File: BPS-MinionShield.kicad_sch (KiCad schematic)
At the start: 78 parts, among them J1 TempConn1, J2 TempConn2, J3 Conn_01x24_Female

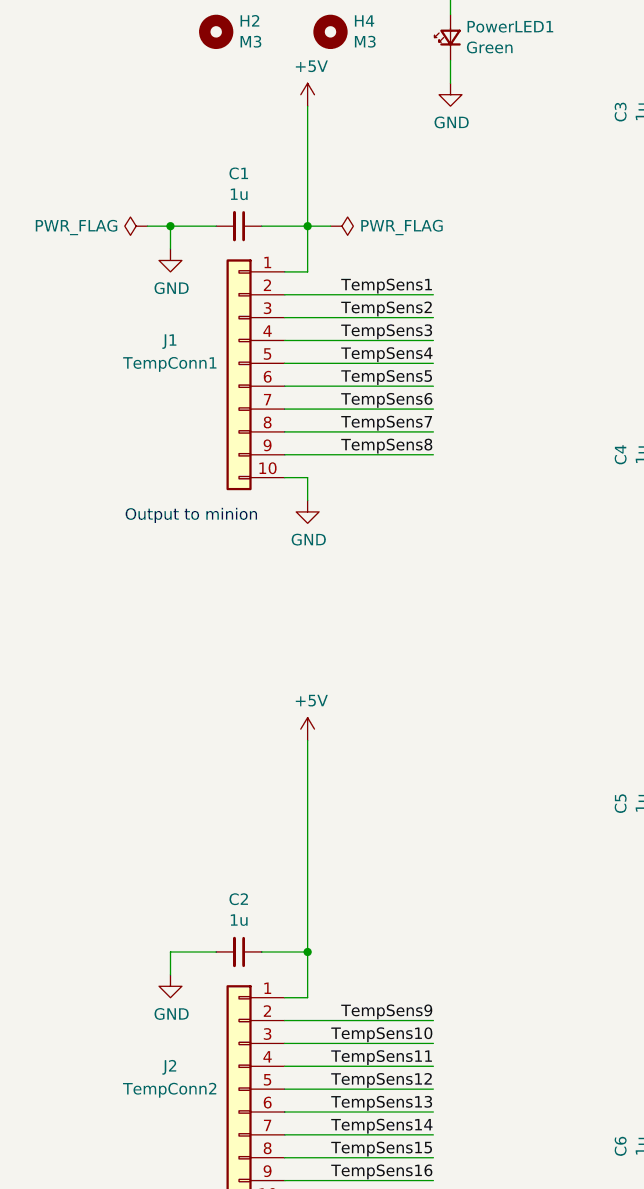
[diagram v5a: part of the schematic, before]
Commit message: move ferrite beads away from connector
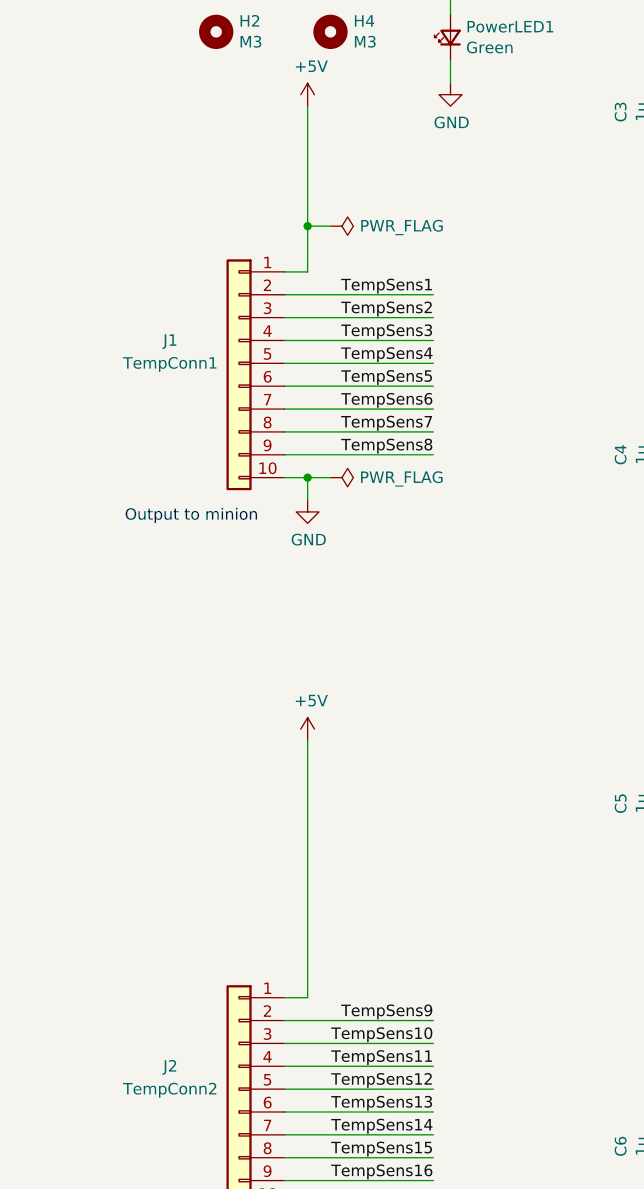
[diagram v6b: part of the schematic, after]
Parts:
- removed C1, C2: 1u, Capacitor_SMD:C_0805_2012Metric_Pad1.18x1.45mm_HandSolder, symbol Device:C_Small
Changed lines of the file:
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@@
   (junction (at 184.15 35.56) (diameter 0) (color 0 0 0 0)
   )
-  (junction (at 48.26 133.985) (diameter 0) (color 0 0 0 0)
-  )
   (junction (at 88.9 73.66) (diameter 0) (color 0 0 0 0)
   )
@@
   (junction (at 152.4 35.56) (diameter 0) (color 0 0 0 0)
   )
-  (junction (at 33.02 53.34) (diameter 0) (color 0 0 0 0)
-  )
   (junction (at 152.4 150.495) (diameter 0) (color 0 0 0 0)
   )
@@
   )
   (junction (at 164.465 35.56) (diameter 0) (color 0 0 0 0)
+  )
+  (junction (at 48.26 81.28) (diameter 0) (color 0 0 0 0)
   )
   (junction (at 229.235 127) (diameter 0) (color 0 0 0 0)
@@
     (stroke (width 0) (type default) (color 0 0 0 0))
   )
-  (wire (pts (xy 33.02 133.985) (xy 33.02 136.525))
-    (stroke (width 0) (type default) (color 0 0 0 0))
-  )
-  (wire (pts (xy 33.02 53.34) (xy 33.02 55.88))
-    (stroke (width 0) (type default) (color 0 0 0 0))
-  )
   (wire (pts (xy 132.715 150.495) (xy 135.255 150.495))
     (stroke (width 0) (type default) (color 0 0 0 0))
@@
     (stroke (width 0) (type default) (color 0 0 0 0))
   )
-  (wire (pts (xy 30.48 53.34) (xy 33.02 53.34))
+  (wire (pts (xy 50.8 81.28) (xy 48.26 81.28))
     (stroke (width 0) (type default) (color 0 0 0 0))
   )
@@
     (stroke (width 0) (type default) (color 0 0 0 0))
   )
-  (wire (pts (xy 48.26 133.985) (xy 48.26 139.065))
-    (stroke (width 0) (type default) (color 0 0 0 0))
-  )
   (wire (pts (xy 91.44 112.395) (xy 88.9 112.395))
     (stroke (width 0) (type default) (color 0 0 0 0))
@@
     (stroke (width 0) (type default) (color 0 0 0 0))
   )
-  (wire (pts (xy 48.26 53.34) (xy 43.18 53.34))
-    (stroke (width 0) (type default) (color 0 0 0 0))
-  )
   (wire (pts (xy 152.4 73.66) (xy 152.4 76.2))
     (stroke (width 0) (type default) (color 0 0 0 0))
@@
     (stroke (width 0) (type default) (color 0 0 0 0))
   )
-  (wire (pts (xy 48.26 133.985) (xy 43.18 133.985))
-    (stroke (width 0) (type default) (color 0 0 0 0))
-  )
   (wire (pts (xy 99.06 73.66) (xy 100.965 73.66))
     (stroke (width 0) (type default) (color 0 0 0 0))
@@
     (stroke (width 0) (type default) (color 0 0 0 0))
   )
-  (wire (pts (xy 48.26 110.49) (xy 48.26 133.985))
+  (wire (pts (xy 48.26 110.49) (xy 48.26 139.065))
     (stroke (width 0) (type default) (color 0 0 0 0))
   )
@@
     (stroke (width 0) (type default) (color 0 0 0 0))
   )
-  (wire (pts (xy 38.1 133.985) (xy 33.02 133.985))
-    (stroke (width 0) (type default) (color 0 0 0 0))
-  )
   (wire (pts (xy 164.465 35.56) (xy 167.005 35.56))
     (stroke (width 0) (type default) (color 0 0 0 0))
@@
   )
   (wire (pts (xy 88.9 35.56) (xy 88.9 38.1))
-    (stroke (width 0) (type default) (color 0 0 0 0))
-  )
-  (wire (pts (xy 38.1 53.34) (xy 33.02 53.34))
     (stroke (width 0) (type default) (color 0 0 0 0))
   )
@@
     (pin "1")
   )
-  (symbol (lib_id "power:GND") (at 33.02 136.525 0) (unit 1)
-    (in_bom yes) (on_board yes)
-    (property "Reference" "#PWR02" (id 0) (at 33.02 142.875 0)
-      (effects (font (size 1.27 1.27)) hide)
-    )
-    (property "Value" "GND" (id 1) (at 33.147 140.9192 0))
-    (property "Footprint" "" (id 2) (at 33.02 136.525 0)
-      (effects (font (size 1.27 1.27)) hide)
-    )
-    (property "Datasheet" "" (id 3) (at 33.02 136.525 0)
-      (effects (font (size 1.27 1.27)) hide)
-    )
-    (pin "1")
-  )
   (symbol (lib_id "Connector_Generic:Conn_01x10") (at 40.64 68.58 0) (mirror y) (unit 1)
     (in_bom yes) (on_board yes)
@@
     (pin "9")
   )
-  (symbol (lib_id "Device:C_Small") (at 40.64 53.34 270) (unit 1)
-    (in_bom yes) (on_board yes)
-    (property "Reference" "C1" (id 0) (at 40.64 47.5234 90))
-    (property "Value" "1u" (id 1) (at 40.64 49.8348 90))
-    (property "Footprint" "Capacitor_SMD:C_0805_2012Metric_Pad1.18x1.45mm_HandSolder" (id 2) (at 40.64 53.34 0)
-      (effects (font (size 1.27 1.27)) hide)
-    )
-    (property "Datasheet" "https://www.mouser.com/ProductDetail/KEMET/C0805C104K5RAC?qs=r%2FVmNO8Tjq4%2F8ymSnGP6Jw%3D%3D" (id 3) (at 40.64 53.34 0)
-      (effects (font (size 1.27 1.27)) hide)
-    )
-    (pin "1")
-    (pin "2")
-  )
-  (symbol (lib_id "power:GND") (at 33.02 55.88 0) (unit 1)
-    (in_bom yes) (on_board yes)
-    (property "Reference" "#PWR01" (id 0) (at 33.02 62.23 0)
-      (effects (font (size 1.27 1.27)) hide)
-    )
-    (property "Value" "GND" (id 1) (at 33.147 60.2742 0))
-    (property "Footprint" "" (id 2) (at 33.02 55.88 0)
-      (effects (font (size 1.27 1.27)) hide)
-    )
-    (property "Datasheet" "" (id 3) (at 33.02 55.88 0)
-      (effects (font (size 1.27 1.27)) hide)
-    )
-    (pin "1")
-  )
   (symbol (lib_id "power:GND") (at 48.26 83.82 0) (unit 1)
     (in_bom yes) (on_board yes)
@@
     (pin "1")
   )
-  (symbol (lib_id "power:PWR_FLAG") (at 30.48 53.34 90) (unit 1)
-    (in_bom yes) (on_board yes)
-    (property "Reference" "#FLG01" (id 0) (at 28.575 53.34 0)
-      (effects (font (size 1.27 1.27)) hide)
-    )
-    (property "Value" "PWR_FLAG" (id 1) (at 27.2542 53.34 90)
+  (symbol (lib_id "power:PWR_FLAG") (at 50.8 81.28 270) (unit 1)
+    (in_bom yes) (on_board yes)
+    (property "Reference" "#FLG01" (id 0) (at 52.705 81.28 0)
+      (effects (font (size 1.27 1.27)) hide)
+    )
+    (property "Value" "PWR_FLAG" (id 1) (at 54.0258 81.28 90)
       (effects (font (size 1.27 1.27)) (justify left))
     )
-    (property "Footprint" "" (id 2) (at 30.48 53.34 0)
-      (effects (font (size 1.27 1.27)) hide)
-    )
-    (property "Datasheet" "~" (id 3) (at 30.48 53.34 0)
+    (property "Footprint" "" (id 2) (at 50.8 81.28 0)
+      (effects (font (size 1.27 1.27)) hide)
+    )
+    (property "Datasheet" "~" (id 3) (at 50.8 81.28 0)
       (effects (font (size 1.27 1.27)) hide)
     )
@@
     (pin "2")
   )
-  (symbol (lib_id "Device:C_Small") (at 40.64 133.985 270) (unit 1)
-    (in_bom yes) (on_board yes)
-    (property "Reference" "C2" (id 0) (at 40.64 128.1684 90))
-    (property "Value" "1u" (id 1) (at 40.64 130.4798 90))
-    (property "Footprint" "Capacitor_SMD:C_0805_2012Metric_Pad1.18x1.45mm_HandSolder" (id 2) (at 40.64 133.985 0)
-      (effects (font (size 1.27 1.27)) hide)
-    )
-    (property "Datasheet" "https://www.mouser.com/ProductDetail/KEMET/C0805C104K5RAC?qs=r%2FVmNO8Tjq4%2F8ymSnGP6Jw%3D%3D" (id 3) (at 40.64 133.985 0)
-      (effects (font (size 1.27 1.27)) hide)
-    )
-    (pin "1")
-    (pin "2")
-  )
   (symbol (lib_id "power:GND") (at 152.4 45.72 0) (unit 1)
     (in_bom yes) (on_board yes)
@@
       (reference "#FLG02") (unit 1) (value "PWR_FLAG") (footprint "")
     )
-    (path "/00000000-0000-0000-0000-00005db6d147"
-      (reference "#PWR01") (unit 1) (value "GND") (footprint "")
-    )
-    (path "/00000000-0000-0000-0000-00005db62854"
-      (reference "#PWR02") (unit 1) (value "GND") (footprint "")
-    )
     (path "/00000000-0000-0000-0000-00005db78fe4"
       (reference "#PWR03") (unit 1) (value "+5V") (footprint "")
@@
       (reference "#PWR0101") (unit 1) (value "GND") (footprint "")
     )
-    (path "/00000000-0000-0000-0000-00005db6d140"
-      (reference "C1") (unit 1) (value "1u") (footprint "Capacitor_SMD:C_0805_2012Metric_Pad1.18x1.45mm_HandSolder")
-    )
-    (path "/7354a4be-ec88-418b-90fe-a8546f86138b"
-      (reference "C2") (unit 1) (value "1u") (footprint "Capacitor_SMD:C_0805_2012Metric_Pad1.18x1.45mm_HandSolder")
-    )
     (path "/0f5e7c1d-b9d8-449c-b2b3-c87304cc4238"

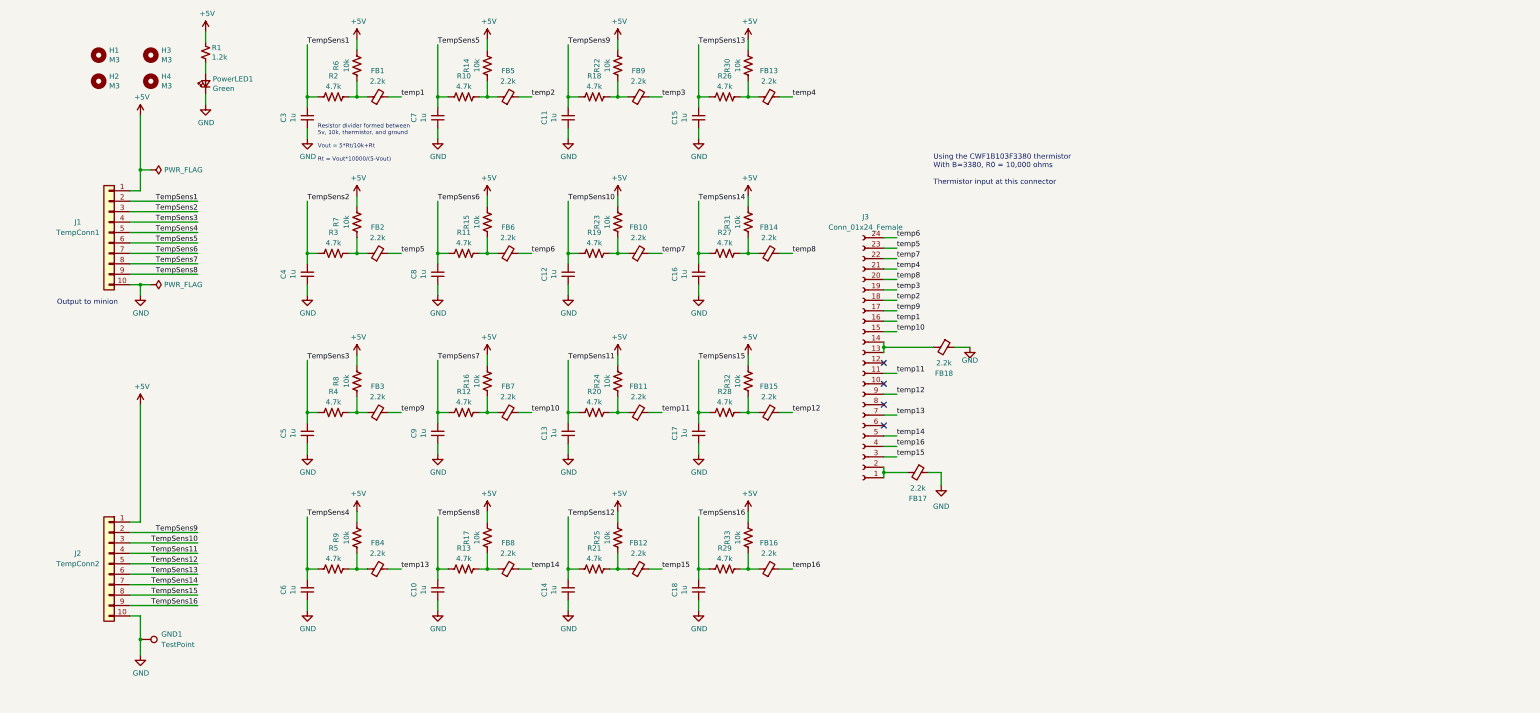
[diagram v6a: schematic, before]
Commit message: change cap values to 100nf
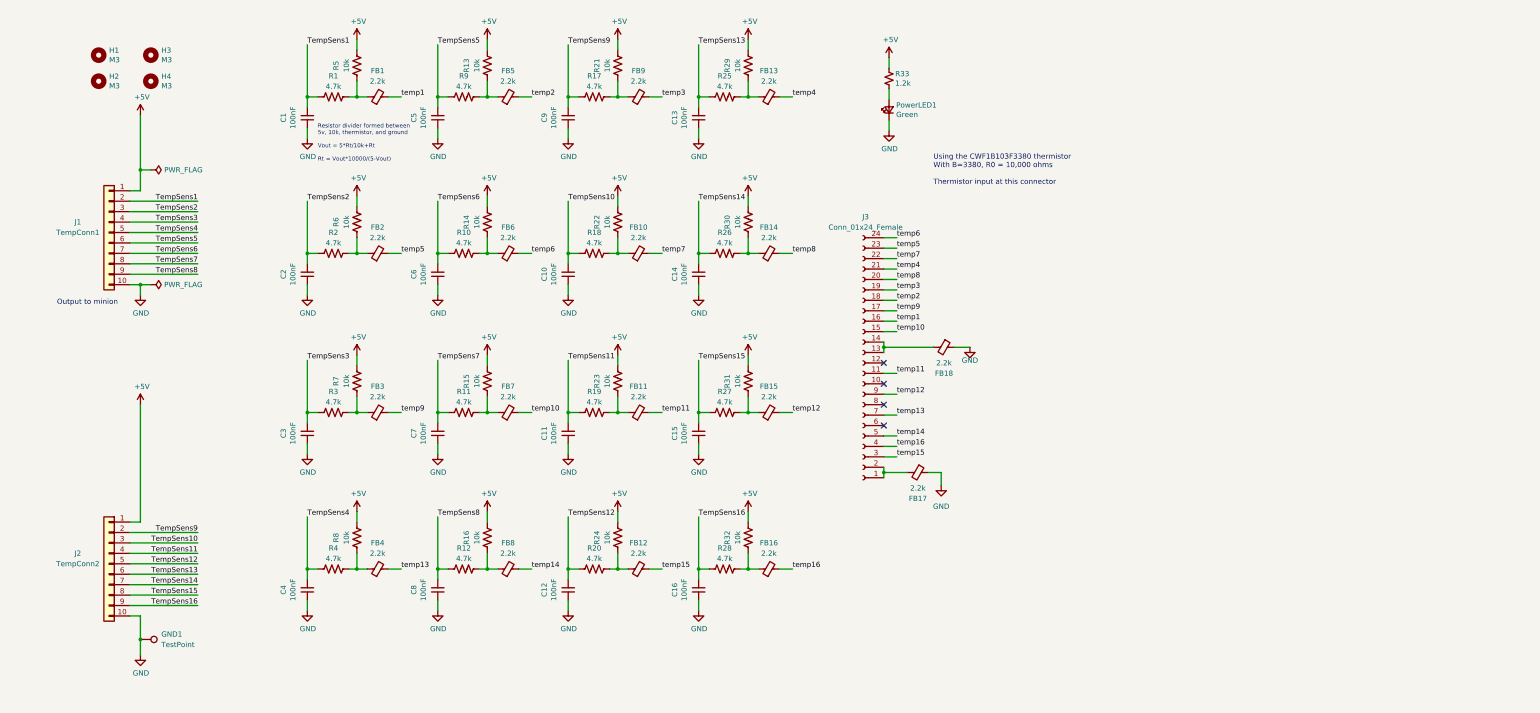
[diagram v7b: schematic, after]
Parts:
- C1: renamed from C3; value 1u -> 100nF
- C10: renamed from C12; value 1u -> 100nF
- C11: renamed from C13; value 1u -> 100nF
- C12: renamed from C14; value 1u -> 100nF
- C13: renamed from C15; value 1u -> 100nF
- C14: renamed from C16; value 1u -> 100nF
- C15: renamed from C17; value 1u -> 100nF
- C16: renamed from C18; value 1u -> 100nF
- C2: renamed from C4; value 1u -> 100nF
- C3: renamed from C5; value 1u -> 100nF
- C4: renamed from C6; value 1u -> 100nF
- C5: renamed from C7; value 1u -> 100nF
- C6: renamed from C8; value 1u -> 100nF
- C7: renamed from C9; value 1u -> 100nF
- C8: renamed from C10; value 1u -> 100nF
- C9: renamed from C11; value 1u -> 100nF
- renumbered R2 to R1, R11 to R10, R12 to R11, R13 to R12, R14 to R13, R15 to R14, R16 to R15, R17 to R16, R18 to R17, R19 to R18, R20 to R19, R3 to R2, R21 to R20, R22 to R21, R23 to R22, R24 to R23, R25 to R24, R26 to R25, R27 to R26, R28 to R27, R29 to R28, R30 to R29, R4 to R3, R31 to R30, R32 to R31, R33 to R32, R1 to R33, R5 to R4, R6 to R5, R7 to R6, R8 to R7, R9 to R8, R10 to R9
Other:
- moved on the sheet: PowerLED1, R33

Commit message: address all tianda requests, start standardization
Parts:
- C1, C10, C11, C12, C13, C14, C15, C16, C2, C3, C4, C5, C6, C7, C8, C9: value 100nF -> 47nF
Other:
- note added: "Change Log: V2.3 Updated PCB routing to reduce GND islands Updated resistor and capacitor values to adjust for LTC startup timing"
- note added: "LTC6811 delay between sleep and measuring ADC voltage is T_WAKE+T_REFUP T_WAKE+T_REFUP = 200us+2.7ms=2.9ms (minimum) freq = 1/.0029 = 345Hz Setting LC cutoff freq to 2*345 = 690 Using a 47nF cap and 4.7K resistor, we achieve a cutoff freq of 720Hz."
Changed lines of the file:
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@@
     (stroke (width 0) (type default))
+  )
+  (text "Change Log:\n\nV2.3\nUpdated PCB routing to reduce GND islands\nUpdated resistor and capacitor values to adjust for LTC startup timing"
+    (at 302.26 38.735 0)
+    (effects (font (size 1.27 1.27)) (justify left bottom))
   )
   (text "Using the CWF1B103F3380 thermistor\nWith B=3380, R0 = 10,000 ohms\n\nThermistor input at this connector"
     (at 241.3 57.15 0)
+    (effects (font (size 1.27 1.27)) (justify left bottom))
+  )
+  (text "LTC6811 delay between sleep and \nmeasuring ADC voltage is T_WAKE+T_REFUP\n\nT_WAKE+T_REFUP = 200us+2.7ms=2.9ms (minimum)\nfreq = 1/.0029 = 345Hz\n\nSetting LC cutoff freq to 2*345 = 690\nUsing a 47nF cap and 4.7K resistor,\nwe achieve a cutoff freq of 720Hz. \n\n\n"
+    (at 227.965 162.56 0)
     (effects (font (size 1.27 1.27)) (justify left bottom))
   )
@@
       (effects (font (size 1.27 1.27)))
     )
-    (property "Value" "100nF" (at 85.3948 40.64 90)
+    (property "Value" "47nF" (at 85.3948 40.64 90)
       (effects (font (size 1.27 1.27)))
     )
@@
       (effects (font (size 1.27 1.27)))
     )
-    (property "Value" "100nF" (at 180.6448 40.64 90)
+    (property "Value" "47nF" (at 180.6448 40.64 90)
       (effects (font (size 1.27 1.27)))
     )
@@
       (effects (font (size 1.27 1.27)))
     )
-    (property "Value" "100nF" (at 180.6448 78.74 90)
+    (property "Value" "47nF" (at 180.6448 78.74 90)
       (effects (font (size 1.27 1.27)))
     )
@@
       (effects (font (size 1.27 1.27)))
     )
-    (property "Value" "100nF" (at 85.3948 78.74 90)
+    (property "Value" "47nF" (at 85.3948 78.74 90)
       (effects (font (size 1.27 1.27)))
     )
@@
       (effects (font (size 1.27 1.27)))
     )
-    (property "Value" "100nF" (at 148.8948 155.575 90)
+    (property "Value" "47nF" (at 148.8948 155.575 90)
       (effects (font (size 1.27 1.27)))
     )
@@
       (effects (font (size 1.27 1.27)))
     )
-    (property "Value" "100nF" (at 180.6448 117.475 90)
+    (property "Value" "47nF" (at 180.6448 117.475 90)
       (effects (font (size 1.27 1.27)))
     )
@@
       (effects (font (size 1.27 1.27)))
     )
-    (property "Value" "100nF" (at 148.8948 40.64 90)
+    (property "Value" "47nF" (at 148.8948 40.64 90)
       (effects (font (size 1.27 1.27)))
     )
@@
       (effects (font (size 1.27 1.27)))
     )
-    (property "Value" "100nF" (at 117.1448 117.475 90)
+    (property "Value" "47nF" (at 117.1448 117.475 90)
       (effects (font (size 1.27 1.27)))
     )
@@
       (effects (font (size 1.27 1.27)))
     )
-    (property "Value" "100nF" (at 117.1448 40.64 90)
+    (property "Value" "47nF" (at 117.1448 40.64 90)
       (effects (font (size 1.27 1.27)))
     )
@@
       (effects (font (size 1.27 1.27)))
     )
-    (property "Value" "100nF" (at 180.6448 155.575 90)
+    (property "Value" "47nF" (at 180.6448 155.575 90)
       (effects (font (size 1.27 1.27)))
     )
@@
       (effects (font (size 1.27 1.27)))
     )
-    (property "Value" "100nF" (at 117.1448 155.575 90)
+    (property "Value" "47nF" (at 117.1448 155.575 90)
       (effects (font (size 1.27 1.27)))
     )
@@
       (effects (font (size 1.27 1.27)))
     )
-    (property "Value" "100nF" (at 85.3948 155.575 90)
+    (property "Value" "47nF" (at 85.3948 155.575 90)
       (effects (font (size 1.27 1.27)))
     )
@@
       (effects (font (size 1.27 1.27)))
     )
-    (property "Value" "100nF" (at 85.3948 117.475 90)
+    (property "Value" "47nF" (at 85.3948 117.475 90)
       (effects (font (size 1.27 1.27)))
     )
@@
       (effects (font (size 1.27 1.27)))
     )
-    (property "Value" "100nF" (at 148.8948 117.475 90)
+    (property "Value" "47nF" (at 148.8948 117.475 90)
       (effects (font (size 1.27 1.27)))
     )
@@
       (effects (font (size 1.27 1.27)))
     )
-    (property "Value" "100nF" (at 117.1448 78.74 90)
+    (property "Value" "47nF" (at 117.1448 78.74 90)
       (effects (font (size 1.27 1.27)))
     )
@@
       (effects (font (size 1.27 1.27)))
     )
-    (property "Value" "100nF" (at 148.8948 78.74 90)
-      (effects (font (size 1.27 1.27)))
-    )
+    (property "Value" "47nF" (at 148.8948 78.74 90)
+      (effects (font (size 1.27 1.27)))
+    )
